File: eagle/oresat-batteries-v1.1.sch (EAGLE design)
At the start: 102 parts, among them IC1 74AHC1G08DBV, J1 2MM-RA-1X8, Q1 CSD16340Q3, Q2 CSD16340Q3, Q3 TPN4R712MD, Q4 TPN4R712MD, Q5 TPN4R712MD, Q6 TPN4R712MD, Q7 CSD16340Q3, U1 LM3761, U10 LTC4412, U11 MAX17055, U12 LTC4412, U13 LTC4412, U14 STM32F042K6, U15 TCAN330, U2 MC74HC1G04DFT1GOSCT, U3 BQ2970, U4 LTC4411, U5 LTC4411, U6 LTC4411, U7 LTC4411, U8 MC74HC1G04DFT1GOSCT, U9 LTC4412, X1 16MHz

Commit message: Updates after design review with Austin. Still some TODOs before layout.
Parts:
- removed TP24, TP25, TP26, TP27, TP28, TP29, TP31, TP32, TP33, TP34, TP35: TP, oresat-batteries:TP
- added R21: 10k, rcl:R-US_R0603
- added TP10: TP, oresat-batteries:TP
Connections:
- new net N$10: TP21.P$1, U14.PA7
- new net N$9: C4.1, R1.1, TP5.P$1, U3.BAT
- net 3.3V: no longer Q7.D, TP22.P$1, TP29.P$1
- net 5V: now also Q7.D, R21.2; no longer C8.1, U11.BATT
- net BATT-: now also IC1P.GND
- net CANH: no longer TP31.P$1, TP34.P$1
- net CANL: no longer TP32.P$1, TP33.P$1
- net CAN_LSTN: now also TP19.P$1
- net CAN_RX: now also TP10.P$1
- net CAN_TX: now also TP22.P$1
- net GND: no longer IC1P.GND
- net HEAT: now also R21.1
- net N$4: now also TP23.P$1
- net NRESET: no longer TP28.P$1
- net STM_DEBUG: no longer TP23.P$1
- net SWCLK: no longer TP27.P$1
- net SWDIO: no longer TP26.P$1
- net SYSSHD: no longer C4.1, R1.1, TP5.P$1, U3.BAT
- net USART2_RX: no longer TP19.P$1, TP24.P$1
- net USART2_TX: no longer TP21.P$1, TP25.P$1
- net VBATT: now also C8.1, U11.BATT
- net VSOLAR: no longer TP35.P$1
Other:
- note added: "CHANGE ME: CHANGE TO P CHANNEL"
- note added: "Iq = 10uA"
- note added: "Iq = 4uA"
- note added: "PCB TRACE HEATER"
- note removed: "Ground Pins"
- moved on the sheet: C4, C8, C9, Q2, Q7, R1, R10, R14, R15, R17, R18, R20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

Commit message: Preliminary layout.
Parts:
- removed J1: 2MM-RA-1X8, oresat-batteries:2MM-RA-1X8
- removed TP6: TP, oresat-batteries:TP
- added J2: CORTEX_DEBUG_PTH, SparkFun-Connectors:CORTEX_DEBUG_PTH
- added TP24: TP, oresat-batteries:TP
- added U$1, U$2: MF-SMDF050, fuse:MF-SMDF050
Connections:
- net COUT renamed BQCOUT
- net N$10 renamed TP21
- net N$3 renamed TEMPSENSE
- net N$5 renamed BGDOUT
- net N$9 renamed BQBAT
- removed net 5V: Q7.D, R21.2
- removed net N$6: D1.C, JP1.8
- removed net STM_DEBUG: J1.8, U14.PA0
- removed net VBATT: B1.V+, C1.1, C2.1, C7.1, C8.1, IC1P.VCC, Q3.D, Q4.D, R1.2, R2.2, R4.2, R6.1, R8.2, TP12.P$1, U1.VIN, U10.VIN, U11.BATT, U2.VCC, U6.OUT, U7.OUT, U8.VCC, U9.VIN
- new net INFUSE: U$1.1, U4.IN, U5.IN
- new net N$14: TP24.P$1, U14.PA0
- new net OUTFUSE: Q5.S, Q6.S, U$2.1, U12.SENSE, U13.SENSE
- new net V_BATT: B1.V+, C1.1, C2.1, C7.1, C8.1, IC1P.VCC, Q3.D, Q4.D, Q7.D, R1.2, R2.2, R21.2, R4.2, R6.1, R8.2, TP12.P$1, U1.VIN, U10.VIN, U11.BATT, U2.VCC, U6.OUT, U7.OUT, U8.VCC, U9.VIN
- net !SHUTDOWN: now also D1.C, JP1.8
- net 3.3V: now also J2.VCC; no longer J1.2
- net GND: now also J2.GND@3, J2.GND@5, J2.GNDDTCT, J2.KEY; no longer J1.1
- net N$16: no longer U13.SENSE
- net NRESET: now also J2.!RESET; no longer J1.3
- net SWCLK: now also J2.SWDCLK/TCK; no longer J1.4
- net SWDIO: now also J2.SWDIO/TMS; no longer J1.5
- net USART2_RX: no longer J1.7
- net USART2_TX: no longer J1.6
- net VSOLAR: now also U$1.2, U$2.2; no longer Q5.S, Q6.S, TP6.P$1, U12.SENSE, U4.IN, U5.IN
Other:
- note added: "3.3V Buck Supply"
- note added: "Ground Clip-Points"
- note removed: "DEBUG"
- note removed: "Fix U$ names"
- moved on the sheet: JP2

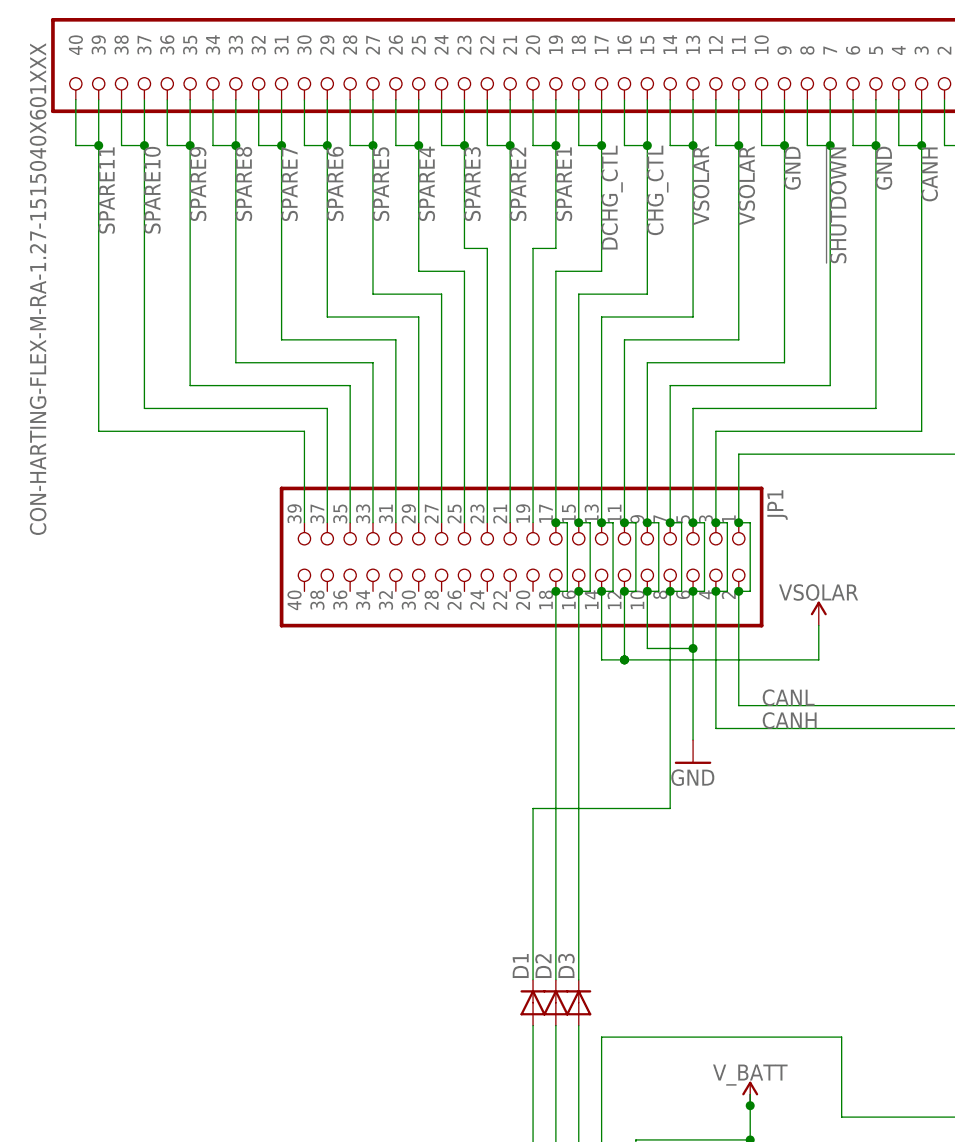
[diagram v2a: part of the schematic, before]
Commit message: Cosmetics, moved all power and signals from gnd layer
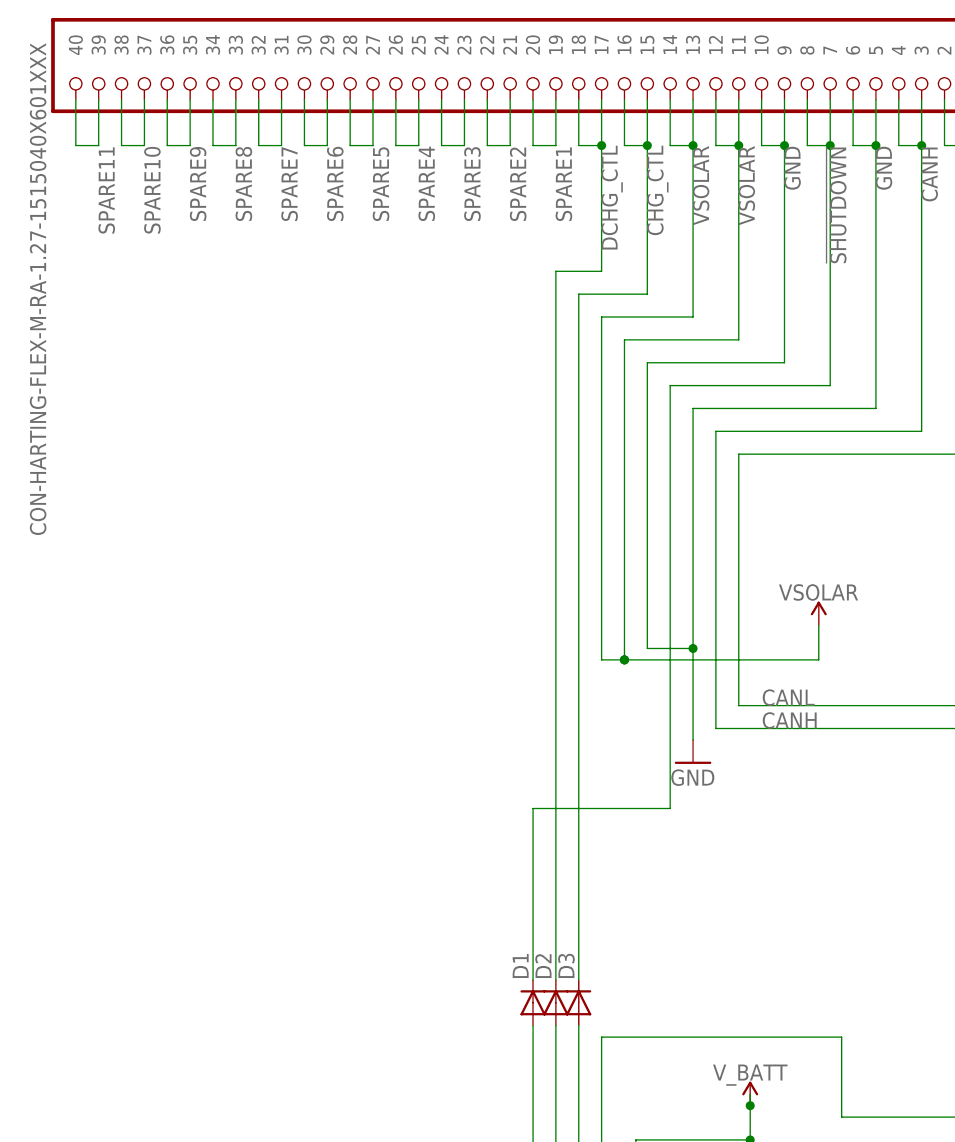
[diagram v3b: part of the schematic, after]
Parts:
- removed JP1: (no value), pinhead:PINHD-2X20
- R7: device rcl:R-US_R0603 -> rcl:R-US_R2512
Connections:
- net !SHUTDOWN: no longer JP1.7, JP1.8
- net CANH: no longer JP1.3, JP1.4
- net CANL: no longer JP1.1, JP1.2
- net CHG_CTL: no longer JP1.15, JP1.16
- net DCHG_CTL: no longer JP1.17, JP1.18
- net GND: no longer JP1.10, JP1.5, JP1.6, JP1.9
- net SPARE1: no longer JP1.19
- net SPARE10: no longer JP1.37
- net SPARE11: no longer JP1.39
- net SPARE2: no longer JP1.21
- net SPARE3: no longer JP1.23
- net SPARE4: no longer JP1.25
- net SPARE5: no longer JP1.27
- net SPARE6: no longer JP1.29
- net SPARE7: no longer JP1.31
- net SPARE8: no longer JP1.33
- net SPARE9: no longer JP1.35
- net VSOLAR: no longer JP1.11, JP1.12, JP1.13, JP1.14
